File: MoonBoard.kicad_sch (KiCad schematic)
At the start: 51 parts, among them Q3 BSS138, SW1 SW_SPST, SW2 SW_DIP_x04, U1 AMS1117-3.3, U2 74LS08, U3 STM32F303CBTx, U5 H5VU25U, Y1 16MHz

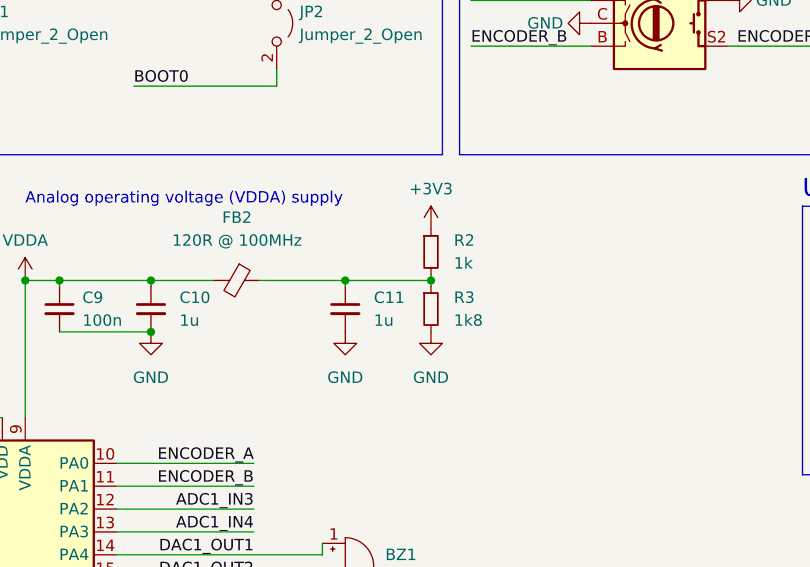
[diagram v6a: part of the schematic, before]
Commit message: update holes
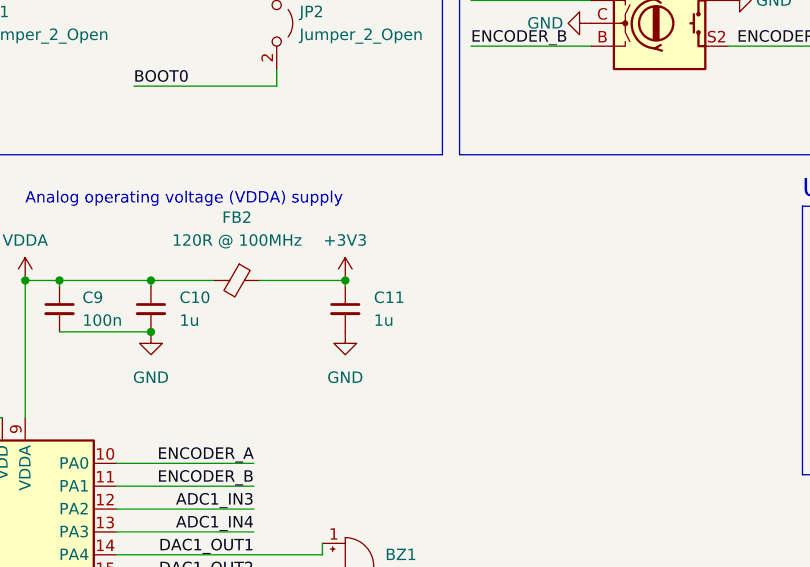
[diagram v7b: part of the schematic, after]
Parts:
- removed R2: 1k, Resistor_SMD:R_0402_1005Metric, symbol Device:R_Small
- removed R3: 1k8, Resistor_SMD:R_0402_1005Metric, symbol Device:R_Small
- H1, H2, H3, H4, H5, H6, H7, H8: footprint MountingHole:MountingHole_2.2mm_M2_Pad_Via -> MoonBoard:2.2mm hole
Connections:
- net +3V3: now also C11.1, FB2.1
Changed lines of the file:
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@@
   (junction (at 28.575 141.605) (diameter 0) (color 0 0 0 0)
   )
-  (junction (at 151.13 94.615) (diameter 0) (color 0 0 0 0)
-  )
   (junction (at 88.265 95.25) (diameter 0) (color 0 0 0 0)
   )
@@
     (stroke (width 0) (type default))
   )
-  (wire (pts (xy 141.605 94.615) (xy 151.13 94.615))
-    (stroke (width 0) (type default))
-  )
   (wire (pts (xy 155.575 68.58) (xy 168.91 68.58))
     (stroke (width 0) (type default))
@@
     (stroke (width 0) (type default))
   )
-  (wire (pts (xy 151.13 93.98) (xy 151.13 94.615))
-    (stroke (width 0) (type default))
-  )
   (wire (pts (xy 28.575 130.175) (xy 28.575 128.905))
     (stroke (width 0) (type default))
@@
     (stroke (width 0) (type default))
   )
-  (wire (pts (xy 151.13 94.615) (xy 151.13 95.25))
-    (stroke (width 0) (type default))
-  )
   (wire (pts (xy 332.74 151.765) (xy 347.98 151.765))
     (stroke (width 0) (type default))
@@
       (effects (font (size 1.27 1.27)) (justify left))
     )
-    (property "Footprint" "MountingHole:MountingHole_2.2mm_M2_Pad_Via" (at 233.045 48.895 0)
+    (property "Footprint" "MoonBoard:2.2mm hole" (at 233.045 48.895 0)
       (effects (font (size 1.27 1.27)) hide)
     )
@@
       (effects (font (size 1.27 1.27)) (justify left))
     )
-    (property "Footprint" "MountingHole:MountingHole_2.2mm_M2_Pad_Via" (at 206.375 60.96 0)
+    (property "Footprint" "MoonBoard:2.2mm hole" (at 206.375 60.96 0)
       (effects (font (size 1.27 1.27)) hide)
     )
@@
       (effects (font (size 1.27 1.27)) (justify left))
     )
-    (property "Footprint" "MountingHole:MountingHole_2.2mm_M2_Pad_Via" (at 233.045 24.765 0)
+    (property "Footprint" "MoonBoard:2.2mm hole" (at 233.045 24.765 0)
       (effects (font (size 1.27 1.27)) hide)
     )
@@
       (effects (font (size 1.27 1.27)) (justify left))
     )
-    (property "Footprint" "MountingHole:MountingHole_2.2mm_M2_Pad_Via" (at 233.045 36.83 0)
+    (property "Footprint" "MoonBoard:2.2mm hole" (at 233.045 36.83 0)
       (effects (font (size 1.27 1.27)) hide)
     )
@@
       (effects (font (size 1.27 1.27)) (justify left))
     )
-    (property "Footprint" "MountingHole:MountingHole_2.2mm_M2_Pad_Via" (at 206.375 36.83 0)
+    (property "Footprint" "MoonBoard:2.2mm hole" (at 206.375 36.83 0)
       (effects (font (size 1.27 1.27)) hide)
     )
@@
       (effects (font (size 1.27 1.27)) (justify left))
     )
-    (property "Footprint" "MountingHole:MountingHole_2.2mm_M2_Pad_Via" (at 233.045 60.96 0)
+    (property "Footprint" "MoonBoard:2.2mm hole" (at 233.045 60.96 0)
       (effects (font (size 1.27 1.27)) hide)
     )
@@
     )
   )
-  (symbol (lib_id "power:GND") (at 151.13 100.33 0) (unit 1)
-    (in_bom yes) (on_board yes) (dnp no) (fields_autoplaced)
-    (property "Reference" "#PWR029" (at 151.13 106.68 0)
-      (effects (font (size 1.27 1.27)) hide)
-    )
-    (property "Value" "GND" (at 151.13 105.41 0)
-      (effects (font (size 1.27 1.27)))
-    )
-    (property "Footprint" "" (at 151.13 100.33 0)
-      (effects (font (size 1.27 1.27)) hide)
-    )
-    (property "Datasheet" "" (at 151.13 100.33 0)
-      (effects (font (size 1.27 1.27)) hide)
-    )
-    (pin "1")
-    (instances
-      (project "MoonBoard"
-        (path "/bb706f4b-6d11-4e29-ae30-1a1ffddaf9f4"
-          (reference "#PWR029") (unit 1)
-        )
-      )
-    )
-  )
   (symbol (lib_id "Transistor_FET:BSS138") (at 163.195 172.085 270) (unit 1)
     (in_bom yes) (on_board yes) (dnp no) (fields_autoplaced)
@@
     )
   )
-  (symbol (lib_id "Device:R_Small") (at 151.13 97.79 0) (unit 1)
-    (in_bom yes) (on_board yes) (dnp no) (fields_autoplaced)
-    (property "Reference" "R3" (at 153.67 96.52 0)
-      (effects (font (size 1.27 1.27)) (justify left))
-    )
-    (property "Value" "1k8" (at 153.67 99.06 0)
-      (effects (font (size 1.27 1.27)) (justify left))
-    )
-    (property "Footprint" "Resistor_SMD:R_0402_1005Metric" (at 151.13 97.79 0)
-      (effects (font (size 1.27 1.27)) hide)
-    )
-    (property "Datasheet" "~" (at 151.13 97.79 0)
-      (effects (font (size 1.27 1.27)) hide)
-    )
-    (pin "1")
-    (pin "2")
-    (instances
-      (project "MoonBoard"
-        (path "/bb706f4b-6d11-4e29-ae30-1a1ffddaf9f4"
-          (reference "R3") (unit 1)
-        )
-      )
-    )
-  )
   (symbol (lib_id "Device:C_Small") (at 136.525 168.275 0) (unit 1)
     (in_bom yes) (on_board yes) (dnp no) (fields_autoplaced)
@@
       (effects (font (size 1.27 1.27)) (justify left))
     )
-    (property "Footprint" "MountingHole:MountingHole_2.2mm_M2_Pad_Via" (at 206.375 24.765 0)
+    (property "Footprint" "MoonBoard:2.2mm hole" (at 206.375 24.765 0)
       (effects (font (size 1.27 1.27)) hide)
     )
@@
     )
   )
-  (symbol (lib_id "power:+3V3") (at 151.13 88.9 0) (unit 1)
+  (symbol (lib_id "power:+3V3") (at 141.605 94.615 0) (unit 1)
     (in_bom yes) (on_board yes) (dnp no)
-    (property "Reference" "#PWR023" (at 151.13 92.71 0)
+    (property "Reference" "#PWR023" (at 141.605 98.425 0)
       (effects (font (size 1.27 1.27)) hide)
     )
-    (property "Value" "+3V3" (at 151.13 84.455 0)
+    (property "Value" "+3V3" (at 141.605 90.17 0)
       (effects (font (size 1.27 1.27)))
     )
-    (property "Footprint" "" (at 151.13 88.9 0)
+    (property "Footprint" "" (at 141.605 94.615 0)
       (effects (font (size 1.27 1.27)) hide)
     )
-    (property "Datasheet" "" (at 151.13 88.9 0)
+    (property "Datasheet" "" (at 141.605 94.615 0)
       (effects (font (size 1.27 1.27)) hide)
     )
@@
       (effects (font (size 1.27 1.27)) (justify left))
     )
-    (property "Footprint" "MountingHole:MountingHole_2.2mm_M2_Pad_Via" (at 206.375 48.895 0)
+    (property "Footprint" "MoonBoard:2.2mm hole" (at 206.375 48.895 0)
       (effects (font (size 1.27 1.27)) hide)
     )
@@
         )
       )
-    )
-  )
-  (symbol (lib_id "Device:R_Small") (at 151.13 91.44 0) (unit 1)
-    (in_bom yes) (on_board yes) (dnp no) (fields_autoplaced)
-    (property "Reference" "R2" (at 153.67 90.17 0)
-      (effects (font (size 1.27 1.27)) (justify left))
-    )
-    (property "Value" "1k" (at 153.67 92.71 0)
-      (effects (font (size 1.27 1.27)) (justify left))
-    )
-    (property "Footprint" "Resistor_SMD:R_0402_1005Metric" (at 151.13 91.44 0)
-      (effects (font (size 1.27 1.27)) hide)
-    )
-    (property "Datasheet" "~" (at 151.13 91.44 0)
-      (effects (font (size 1.27 1.27)) hide)
-    )
-    (pin "1")
-    (pin "2")
-    (instances
-      (project "MoonBoard"
-        (path "/bb706f4b-6d11-4e29-ae30-1a1ffddaf9f4"
-          (reference "R2") (unit 1)
-        )
-      )

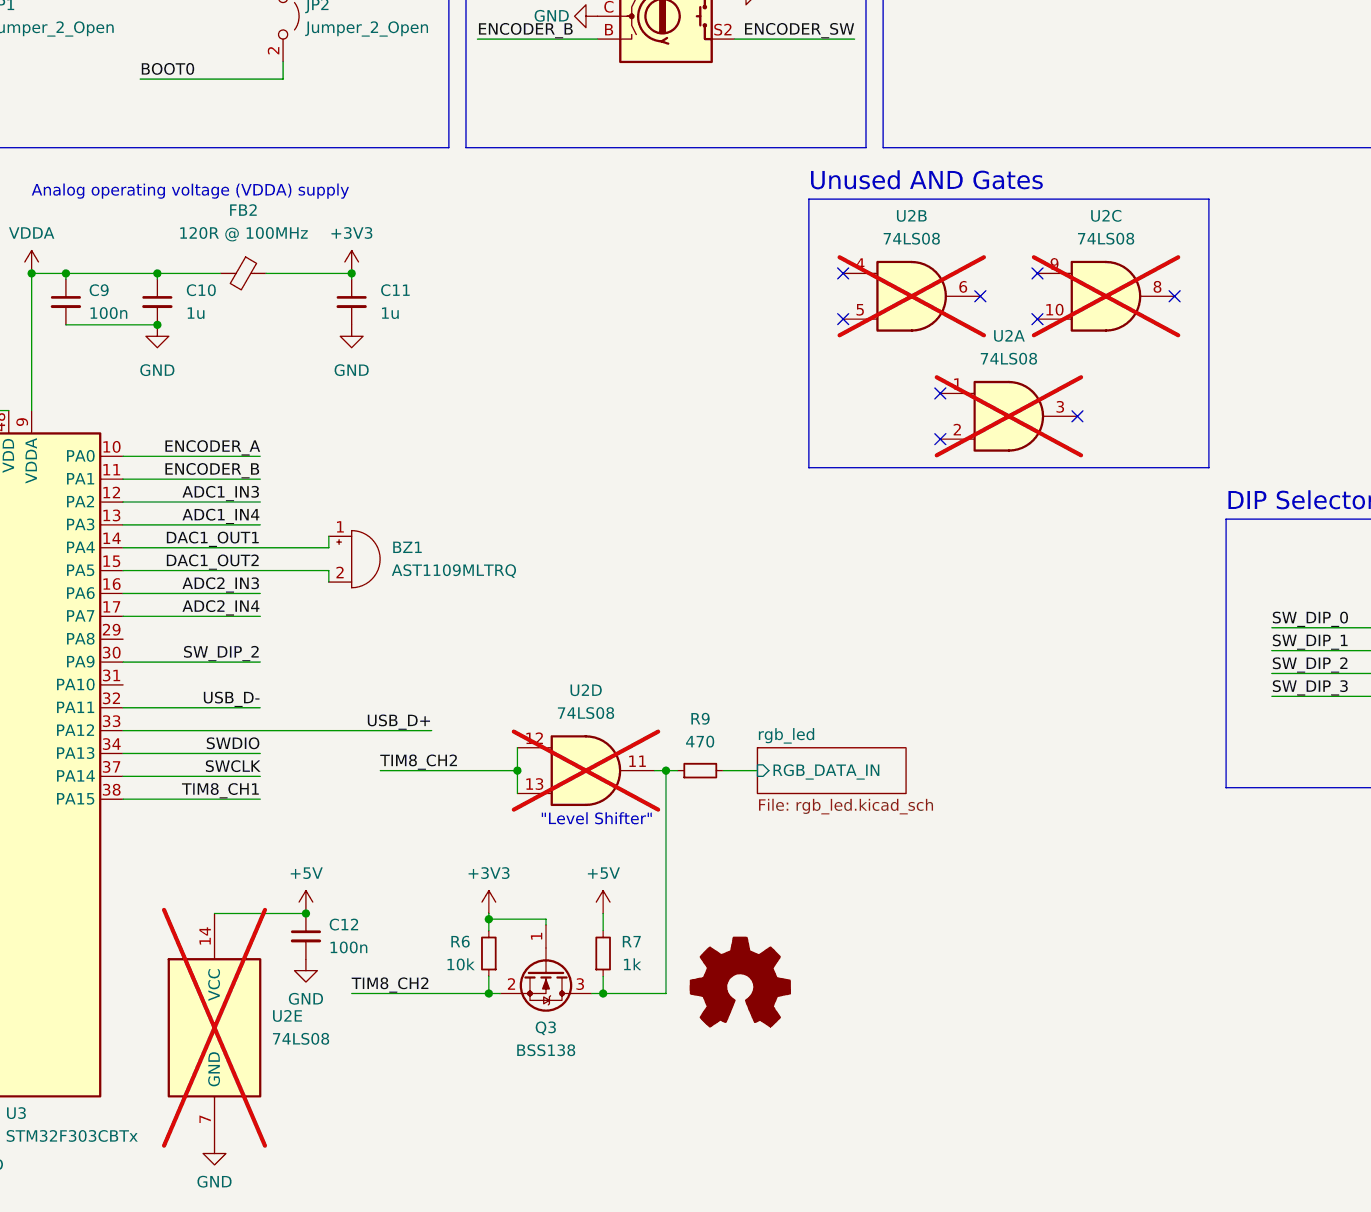
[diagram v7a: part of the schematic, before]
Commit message: remove bad level shifter
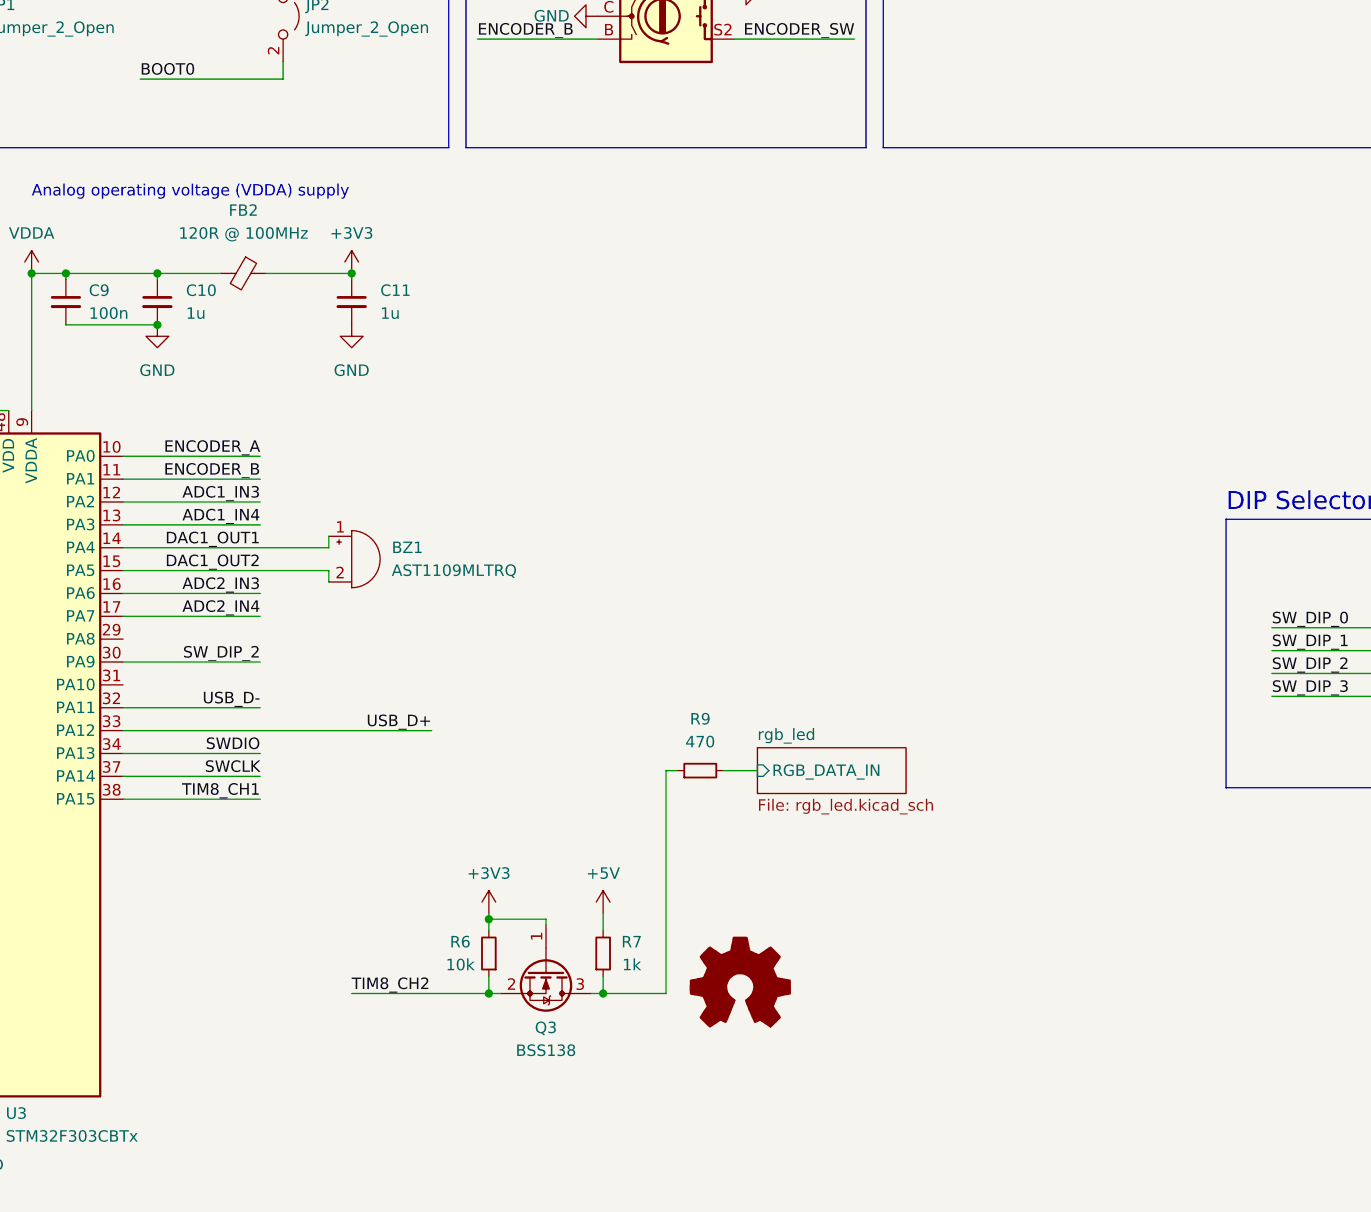
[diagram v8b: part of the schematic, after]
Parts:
- removed C12: 100n, Capacitor_SMD:C_0402_1005Metric, symbol Device:C_Small
- removed U2: 74LS08, Package_SO:SOIC-14_3.9x8.7mm_P1.27mm, symbol 74xx:74LS08
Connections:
- no-connect marks 16 -> 7
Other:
- note removed: ""Level Shifter""
- note removed: "Unused AND Gates"
